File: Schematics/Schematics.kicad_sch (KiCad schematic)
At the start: 9 parts, among them J1 Conn_01x02_Female, U1 TP4056, U2 NRF52840-DONGLE, U3 BU30TD3WG

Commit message: Edited schematic
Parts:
- added C?: 0.47u, symbol pspice:CAP
- added U?: BME688, symbol BME688:BME688
- added U?: LIS3DH, symbol LIS3DH:LIS3DH
- C1: value 47u -> 0.47u
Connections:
- net GND: now also C?.2
- net VBUS: no longer U?.5 (VCC)
- net VOUT: now also U?.5 (VCC), C?.1
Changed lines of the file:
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@@
   (junction (at 144.78 121.92) (diameter 0) (color 0 0 0 0)
+  )
+  (junction (at 190.5 116.84) (diameter 0) (color 0 0 0 0)
   )
   (no_connect (at 146.05 96.52))
@@
     (stroke (width 0) (type default) (color 0 0 0 0))
   )
+  (wire (pts (xy 190.5 116.84) (xy 186.69 116.84))
+    (stroke (width 0) (type default) (color 0 0 0 0))
+  )
   (wire (pts (xy 95.25 104.14) (xy 99.06 104.14))
     (stroke (width 0) (type default) (color 0 0 0 0))
@@
     (stroke (width 0) (type default) (color 0 0 0 0))
   )
+  (wire (pts (xy 194.31 116.84) (xy 190.5 116.84))
+    (stroke (width 0) (type default) (color 0 0 0 0))
+  )
   (wire (pts (xy 140.97 52.07) (xy 140.97 66.04))
     (stroke (width 0) (type default) (color 0 0 0 0))
@@
   )
   (wire (pts (xy 148.59 53.34) (xy 152.4 53.34))
+    (stroke (width 0) (type default) (color 0 0 0 0))
+  )
+  (wire (pts (xy 190.5 129.54) (xy 190.5 132.08))
     (stroke (width 0) (type default) (color 0 0 0 0))
   )
@@
     )
   )
-  (global_label "VBUS" (shape input) (at 152.4 53.34 0) (fields_autoplaced)
+  (global_label "VOUT" (shape input) (at 152.4 53.34 0) (fields_autoplaced)
     (effects (font (size 1.27 1.27)) (justify left))
-    (property "Intersheet References" "${INTERSHEET_REFS}" (id 0) (at 159.7117 53.2606 0)
+    (property "Intersheet References" "${INTERSHEET_REFS}" (id 0) (at 159.5302 53.2606 0)
       (effects (font (size 1.27 1.27)) (justify left) hide)
     )
   )
-  (global_label "VOUT" (shape output) (at 186.69 116.84 0) (fields_autoplaced)
+  (global_label "VOUT" (shape output) (at 194.31 116.84 0) (fields_autoplaced)
     (effects (font (size 1.27 1.27)) (justify left))
-    (property "Intersheet References" "${INTERSHEET_REFS}" (id 0) (at 193.8202 116.7606 0)
+    (property "Intersheet References" "${INTERSHEET_REFS}" (id 0) (at 201.4402 116.7606 0)
       (effects (font (size 1.27 1.27)) (justify left) hide)
     )
@@
     (in_bom yes) (on_board yes)
     (property "Reference" "C1" (id 0) (at 151.13 106.68 90))
-    (property "Value" "47u" (id 1) (at 151.13 109.22 90))
+    (property "Value" "0.47u" (id 1) (at 151.13 109.22 90))
     (property "Footprint" "" (id 2) (at 151.13 114.3 0)
       (effects (font (size 1.27 1.27)) hide)
@@
     )
     (property "Datasheet" "" (id 3) (at 146.05 54.61 0)
+      (effects (font (size 1.27 1.27)) hide)
+    )
+    (pin "1")
+  )
+  (symbol (lib_id "power:GND") (at 190.5 132.08 0) (unit 1)
+    (in_bom yes) (on_board yes) (fields_autoplaced)
+    (property "Reference" "#PWR?" (id 0) (at 190.5 138.43 0)
+      (effects (font (size 1.27 1.27)) hide)
+    )
+    (property "Value" "GND" (id 1) (at 190.5 137.16 0))
+    (property "Footprint" "" (id 2) (at 190.5 132.08 0)
+      (effects (font (size 1.27 1.27)) hide)
+    )
+    (property "Datasheet" "" (id 3) (at 190.5 132.08 0)
       (effects (font (size 1.27 1.27)) hide)
     )
@@
     (pin "5")
   )
+  (symbol (lib_id "BME688:BME688") (at 175.26 38.1 0) (unit 1)
+    (in_bom yes) (on_board yes) (fields_autoplaced)
+    (property "Reference" "U?" (id 0) (at 185.42 41.2749 0)
+      (effects (font (size 1.27 1.27)) (justify left))
+    )
+    (property "Value" "BME688" (id 1) (at 185.42 43.8149 0)
+      (effects (font (size 1.27 1.27)) (justify left))
+    )
+    (property "Footprint" "" (id 2) (at 175.26 38.1 0)
+      (effects (font (size 1.27 1.27)) hide)
+    )
+    (property "Datasheet" "" (id 3) (at 175.26 38.1 0)
+      (effects (font (size 1.27 1.27)) hide)
+    )
+    (pin "1")
+    (pin "2")
+    (pin "3")
+    (pin "4")
+    (pin "5")
+  )
   (symbol (lib_id "Device:R") (at 168.91 92.71 0) (unit 1)
     (in_bom yes) (on_board yes) (fields_autoplaced)
@@
     (pin "1")
     (pin "2")
+  )
+  (symbol (lib_id "LIS3DH:LIS3DH") (at 201.93 39.37 0) (unit 1)
+    (in_bom yes) (on_board yes) (fields_autoplaced)
+    (property "Reference" "U?" (id 0) (at 213.36 35.56 0))
+    (property "Value" "LIS3DH" (id 1) (at 213.36 38.1 0))
+    (property "Footprint" "" (id 2) (at 201.93 39.37 0)
+      (effects (font (size 1.27 1.27)) hide)
+    )
+    (property "Datasheet" "" (id 3) (at 201.93 39.37 0)
+      (effects (font (size 1.27 1.27)) hide)
+    )
+    (pin "1")
+    (pin "10")
+    (pin "11")
+    (pin "2")
+    (pin "3")
+    (pin "4")
+    (pin "5")
+    (pin "6")
+    (pin "7")
+    (pin "8")
+    (pin "9")
   )
   (symbol (lib_id "NRF52840-DONGLE:NRF52840-DONGLE") (at 138.43 81.28 90) (unit 1)
@@
     (pin "VBUS")
   )
+  (symbol (lib_id "pspice:CAP") (at 190.5 123.19 0) (unit 1)
+    (in_bom yes) (on_board yes)
+    (property "Reference" "C?" (id 0) (at 182.88 123.19 90))
+    (property "Value" "0.47u" (id 1) (at 185.42 123.19 90))
+    (property "Footprint" "" (id 2) (at 190.5 123.19 0)
+      (effects (font (size 1.27 1.27)) hide)
+    )
+    (property "Datasheet" "~" (id 3) (at 190.5 123.19 0)
+      (effects (font (size 1.27 1.27)) hide)
+    )
+    (pin "1")
+    (pin "2")
+  )
   (symbol (lib_id "TP4056_module:TP4056") (at 118.11 101.6 0) (unit 1)
     (in_bom yes) (on_board yes)
@@
       (reference "#PWR?") (unit 1) (value "GND") (footprint "")
     )
+    (path "/4245e3d4-5ae2-4063-8c15-490429326602"
+      (reference "#PWR?") (unit 1) (value "GND") (footprint "")
+    )
     (path "/23c12ffd-c917-4e40-9f45-ae4044d3a796"
-      (reference "C1") (unit 1) (value "47u") (footprint "")
+      (reference "C1") (unit 1) (value "0.47u") (footprint "")
+    )
+    (path "/eb68cc29-b9b2-434d-9324-08f8124ad2a3"
+      (reference "C?") (unit 1) (value "0.47u") (footprint "")
     )
     (path "/5256f389-7a72-40b1-a071-efe64c49e98f"
@@
       (reference "U?") (unit 1) (value "BH1750") (footprint "")
     )
-  )
+    (path "/826c3af9-eceb-4f6b-a112-627c545a279c"
+      (reference "U?") (unit 1) (value "BME688") (footprint "")
+    )
+    (path "/a9d65e80-5655-467a-8484-75492741f3e4"
+      (reference "U?") (unit 1) (value "LIS3DH") (footprint "")
+    )
+  )

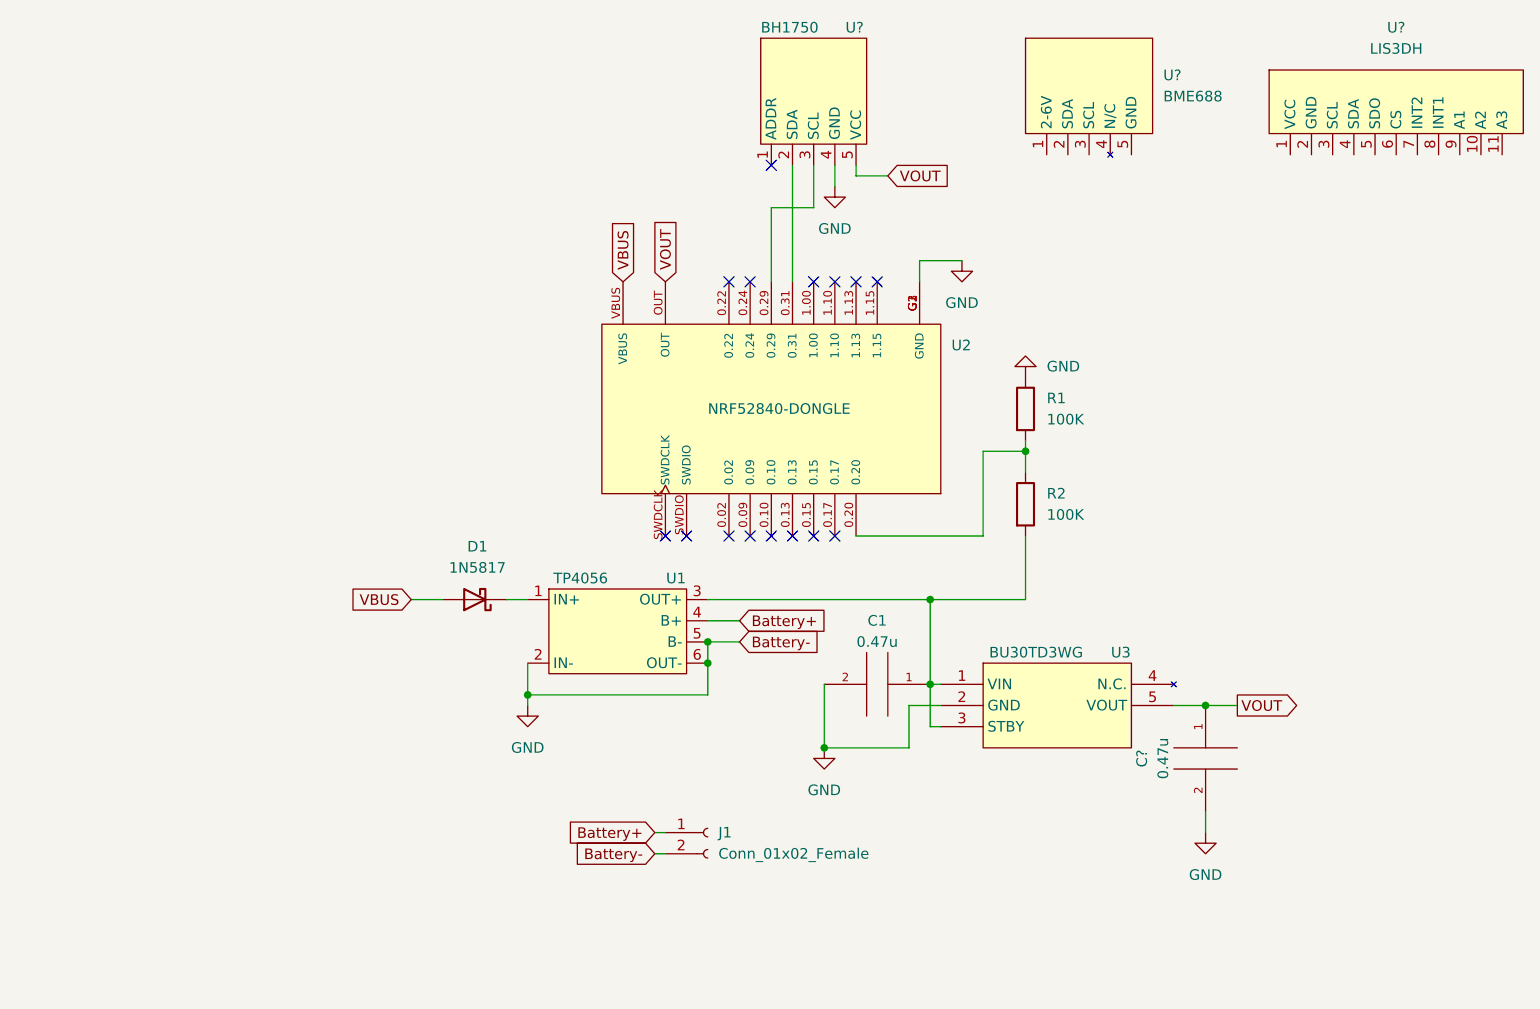
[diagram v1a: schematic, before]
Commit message: Fixed schematic
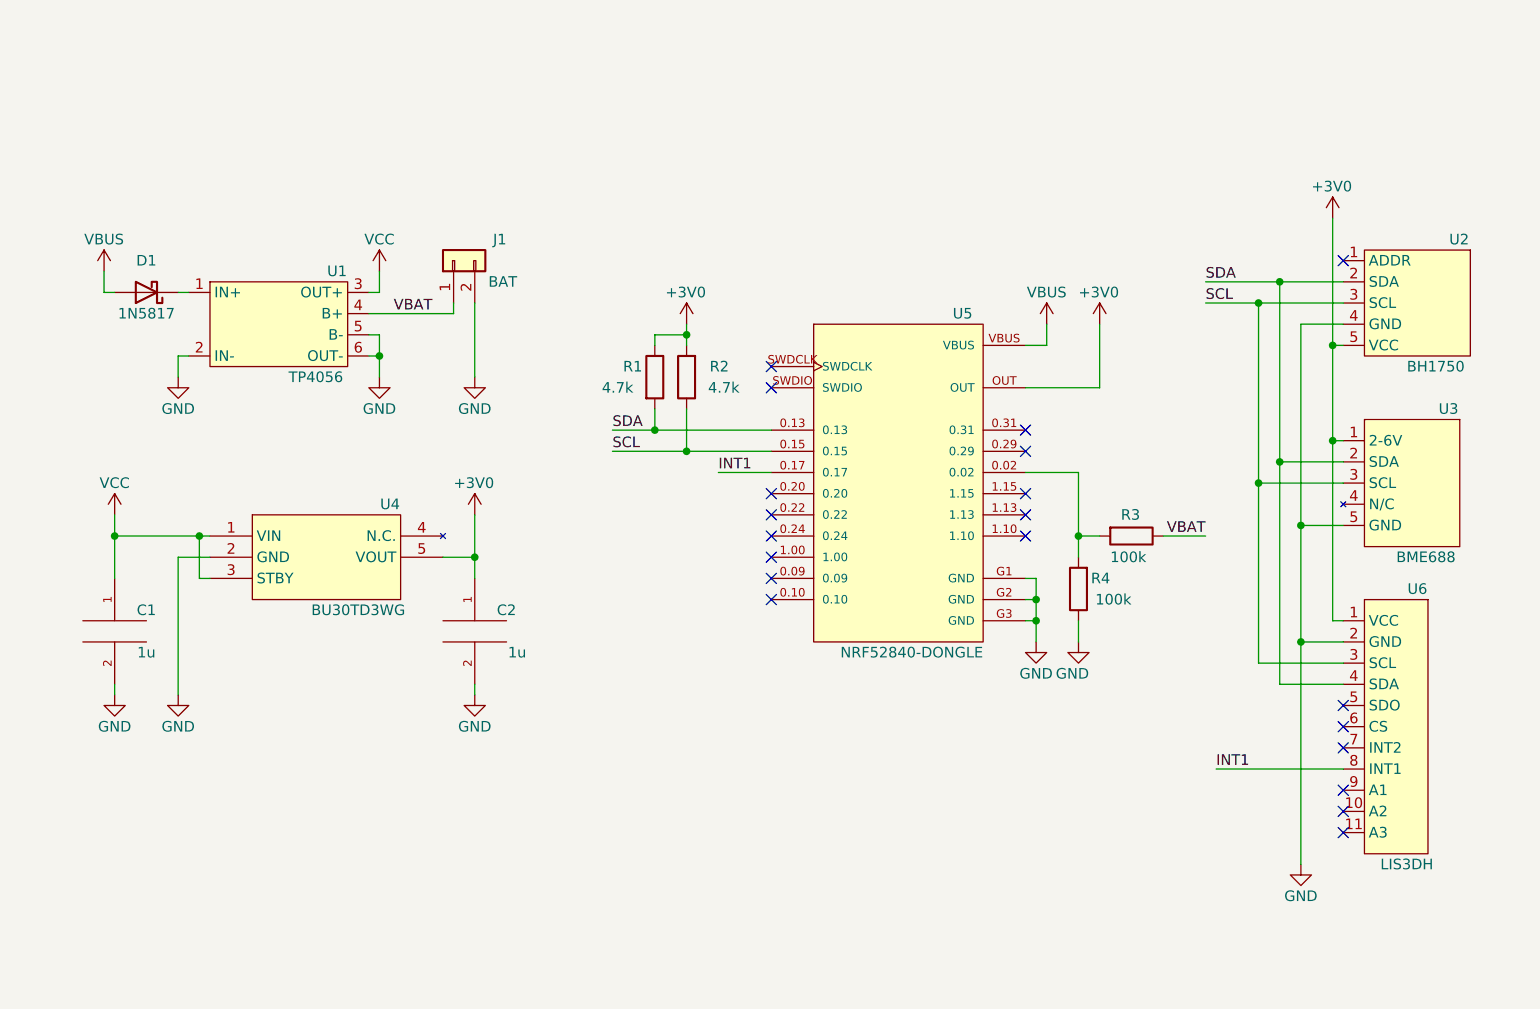
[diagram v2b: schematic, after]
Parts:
- removed C?: 0.47u, symbol pspice:CAP
- removed J1: Conn_01x02_Female, symbol Connector:Conn_01x02_Female
- removed U2: NRF52840-DONGLE, MODULE_NRF52840-DONGLE, symbol NRF52840-DONGLE:NRF52840-DONGLE
- removed U3: BU30TD3WG, symbol BU30TD3WG:BU30TD3WG
- removed U?: BH1750, symbol BH1750:BH1750
- removed U?: BME688, symbol BME688:BME688
- removed U?: LIS3DH, symbol LIS3DH:LIS3DH
- added C2: 1u, Capacitor_THT:C_Disc_D5.1mm_W3.2mm_P5.00mm, symbol pspice:CAP
- added J1: BAT, symbol Connector_Generic:Conn_01x02
- added R3, R4: 100k, Resistor_THT:R_Axial_DIN0207_L6.3mm_D2.5mm_P10.16mm_Horizontal, symbol Device:R
- added U2: BH1750, symbol BH1750:BH1750
- added U3: BME688, symbol BME688:BME688
- added U4: BU30TD3WG, Package_TO_SOT_SMD:SOT-23-5, symbol BU30TD3WG:BU30TD3WG
- added U5: NRF52840-DONGLE, symbol NRF52840-DONGLE:NRF52840-DONGLE
- added U6: LIS3DH, symbol LIS3DH:LIS3DH
- C1: value 0.47u -> 1u; footprint (none) -> Capacitor_THT:C_Disc_D5.1mm_W3.2mm_P5.00mm
- R1, R2: value 100K -> 4.7k; footprint (none) -> Resistor_THT:R_Axial_DIN0207_L6.3mm_D2.5mm_P10.16mm_Horizontal
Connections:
- net GND: now also C2.2, J1.2 (Pin_2), R4.1, U2.4 (GND), U3.5 (GND), U4.2 (GND), U5.G1 (GND), U5.G2 (GND), U5.G3 (GND), U6.2 (GND); no longer R1.1
- net VBUS: now also U5.VBUS
- net SCL: now reaches R2.1
- net SCL: now also U2.3 (SCL), U3.3 (SCL), U5.0.15, U6.3 (SCL); no longer R1.2
- net VCC: now reaches C1.1, U1.3 (OUT+)
- net VCC: now also U4.1 (VIN), U4.3 (STBY); no longer R2.2
- net Battery+ renamed VBAT
- net VBAT: now also J1.1 (Pin_1), R3.1
- new net: R3.2, R4.2, U5.0.02
- new net +3V0: C2.1, R1.1, R2.2, U2.5 (VCC), U3.1 (2-6V), U4.5 (VOUT), U5.OUT, U6.1 (VCC)
- new net INT1: U5.0.17, U6.8 (INT1)
- new net SDA: R1.2, U2.2 (SDA), U3.2 (SDA), U5.0.13, U6.4 (SDA)
- no-connect marks 15 -> 20

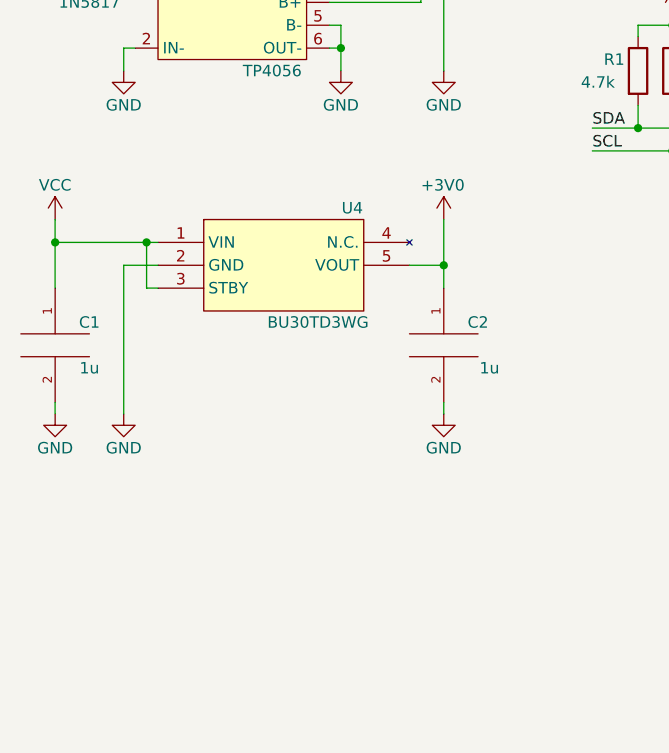
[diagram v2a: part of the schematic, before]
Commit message: Changed some footprints and started the pcb development
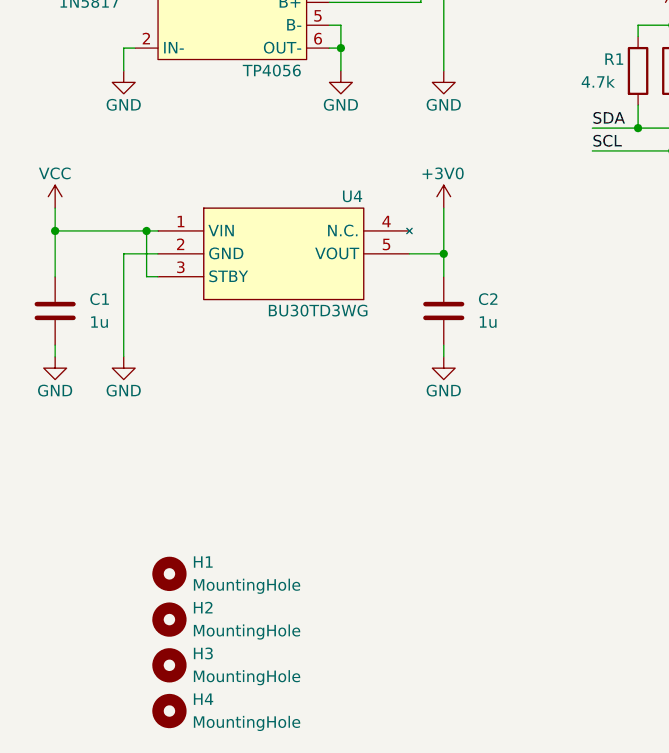
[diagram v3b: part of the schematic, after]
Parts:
- removed C1, C2: 1u, Capacitor_THT:C_Disc_D5.1mm_W3.2mm_P5.00mm, symbol pspice:CAP
- added C1, C2: 1u, Capacitor_THT:C_Disc_D5.1mm_W3.2mm_P5.00mm, symbol Device:C
- added H1, H2, H3, H4: MountingHole, MountingHole:MountingHole_2.5mm, symbol Mechanical:MountingHole
- J1: footprint (none) -> custom:KLS5-18650-005
- U1: footprint (none) -> custom:TP4056-18650
- U2: footprint (none) -> custom:BH1750
- U3: footprint (none) -> custom:BME688
- U5: footprint (none) -> custom:MODULE_NRF52840-DONGLE
- U6: footprint (none) -> custom:LIS3DH
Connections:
- net +3V0: now also C2.1
- net GND: now also C1.2, C2.2
- net VCC: now also C1.1
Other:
- moved on the sheet: U4

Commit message: Uploading Modified Schematic with PCB version 1
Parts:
- removed J1: BAT, custom:KLS5-18650-005, symbol Connector_Generic:Conn_01x02
- added BT1: 3.7V Li-ion, custom:KLS5-18650-005, symbol Device:Battery
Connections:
- net GND: now also BT1.2 (-)
- net VBAT: now also BT1.1 (+)
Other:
- moved on the sheet: C1, C2, D1, U1, U4

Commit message: Added a couple prototypes for a pcb
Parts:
- R1, R2, R3, R4: footprint Resistor_THT:R_Axial_DIN0207_L6.3mm_D2.5mm_P10.16mm_Horizontal -> Resistor_THT:R_Axial_DIN0204_L3.6mm_D1.6mm_P5.08mm_Horizontal
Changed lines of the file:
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@@
       (effects (font (size 1.27 1.27)) (justify left))
     )
-    (property "Footprint" "Resistor_THT:R_Axial_DIN0207_L6.3mm_D2.5mm_P10.16mm_Horizontal" (id 2) (at 122.682 77.47 90)
+    (property "Footprint" "Resistor_THT:R_Axial_DIN0204_L3.6mm_D1.6mm_P5.08mm_Horizontal" (id 2) (at 122.682 77.47 90)
       (effects (font (size 1.27 1.27)) hide)
     )
@@
       (effects (font (size 1.27 1.27)) (justify left))
     )
-    (property "Footprint" "Resistor_THT:R_Axial_DIN0207_L6.3mm_D2.5mm_P10.16mm_Horizontal" (id 2) (at 177.038 102.87 90)
+    (property "Footprint" "Resistor_THT:R_Axial_DIN0204_L3.6mm_D1.6mm_P5.08mm_Horizontal" (id 2) (at 177.038 102.87 90)
       (effects (font (size 1.27 1.27)) hide)
     )
@@
       (effects (font (size 1.27 1.27)) (justify left))
     )
-    (property "Footprint" "Resistor_THT:R_Axial_DIN0207_L6.3mm_D2.5mm_P10.16mm_Horizontal" (id 2) (at 181.61 94.742 90)
+    (property "Footprint" "Resistor_THT:R_Axial_DIN0204_L3.6mm_D1.6mm_P5.08mm_Horizontal" (id 2) (at 181.61 94.742 90)
       (effects (font (size 1.27 1.27)) hide)
     )
@@
       (effects (font (size 1.27 1.27)) (justify left))
     )
-    (property "Footprint" "Resistor_THT:R_Axial_DIN0207_L6.3mm_D2.5mm_P10.16mm_Horizontal" (id 2) (at 130.048 77.47 90)
+    (property "Footprint" "Resistor_THT:R_Axial_DIN0204_L3.6mm_D1.6mm_P5.08mm_Horizontal" (id 2) (at 130.048 77.47 90)
       (effects (font (size 1.27 1.27)) hide)
     )
@@
     )
     (path "/24a5c655-6fd5-46ec-b259-a9195b8b1f09"
-      (reference "R1") (unit 1) (value "4.7k") (footprint "Resistor_THT:R_Axial_DIN0207_L6.3mm_D2.5mm_P10.16mm_Horizontal")
+      (reference "R1") (unit 1) (value "4.7k") (footprint "Resistor_THT:R_Axial_DIN0204_L3.6mm_D1.6mm_P5.08mm_Horizontal")
     )
     (path "/c08cba8b-bd47-4377-8d81-2becb4163cc7"
-      (reference "R2") (unit 1) (value "4.7k") (footprint "Resistor_THT:R_Axial_DIN0207_L6.3mm_D2.5mm_P10.16mm_Horizontal")
+      (reference "R2") (unit 1) (value "4.7k") (footprint "Resistor_THT:R_Axial_DIN0204_L3.6mm_D1.6mm_P5.08mm_Horizontal")
     )
     (path "/66cf8161-13c1-4990-aa00-ab3e4f55de4b"
-      (reference "R3") (unit 1) (value "100k") (footprint "Resistor_THT:R_Axial_DIN0207_L6.3mm_D2.5mm_P10.16mm_Horizontal")
+      (reference "R3") (unit 1) (value "100k") (footprint "Resistor_THT:R_Axial_DIN0204_L3.6mm_D1.6mm_P5.08mm_Horizontal")
     )
     (path "/39234ff8-bcb6-4eca-9b90-eb145920db1f"
-      (reference "R4") (unit 1) (value "100k") (footprint "Resistor_THT:R_Axial_DIN0207_L6.3mm_D2.5mm_P10.16mm_Horizontal")
+      (reference "R4") (unit 1) (value "100k") (footprint "Resistor_THT:R_Axial_DIN0204_L3.6mm_D1.6mm_P5.08mm_Horizontal")
     )
     (path "/c50b859c-4113-4516-83a7-92a0814b7e6e"

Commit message: Created new versions of the pcb and generated gerber/drill files
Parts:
- BT1: footprint custom:KLS5-18650-005 -> custom:BHC-18650-1P
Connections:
- net GND: no longer BT1.2 (-), U1.5 (B-)
- net INT1: now also U5.1.10; no longer U5.0.17
- net VCC: now also R3.1
- net VBAT: no longer names the net of BT1.1 (+), U1.4 (B+)
- net VBAT: no longer R3.1
- new net: BT1.2 (-), U1.5 (B-)
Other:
- moved on the sheet: BT1, R3, R4

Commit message: Created final variant of the pcb, moved the schematic of the main node in this folder, modified the schematic of the main node
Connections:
- net GND renamed GNDD
